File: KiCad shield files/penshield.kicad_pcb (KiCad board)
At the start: 2 copper layers, 55.9 x 16.5 mm, 7 parts

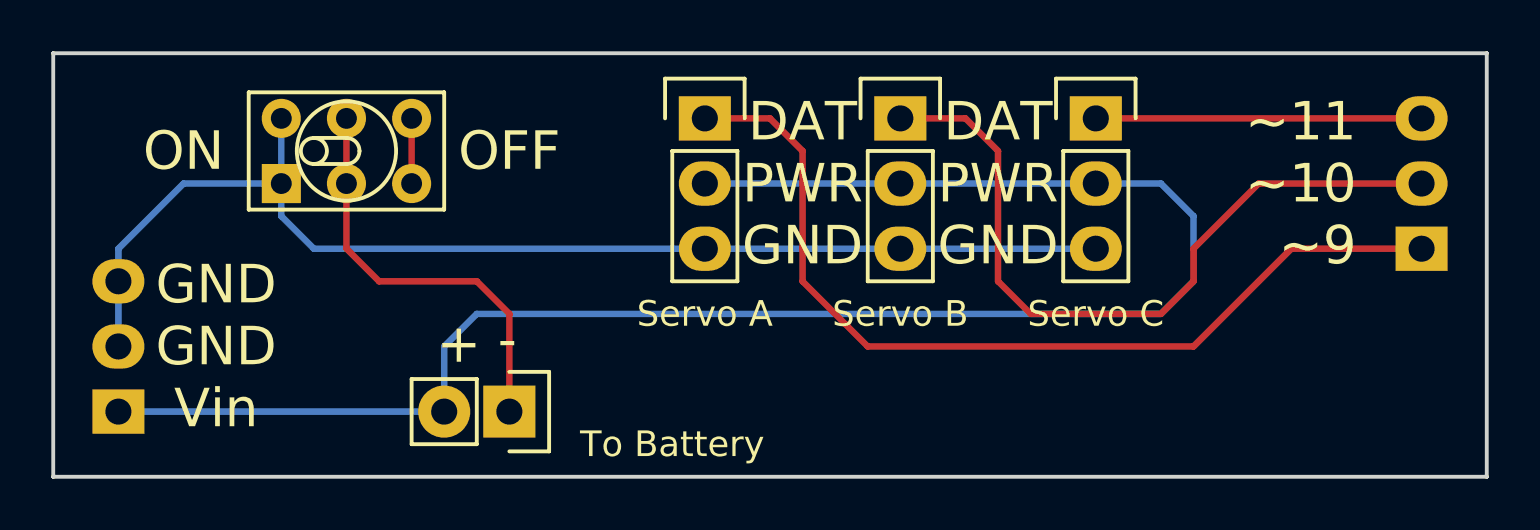
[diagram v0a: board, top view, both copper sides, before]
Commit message: Updated KiCad project; fixed spacing of header pins on shield
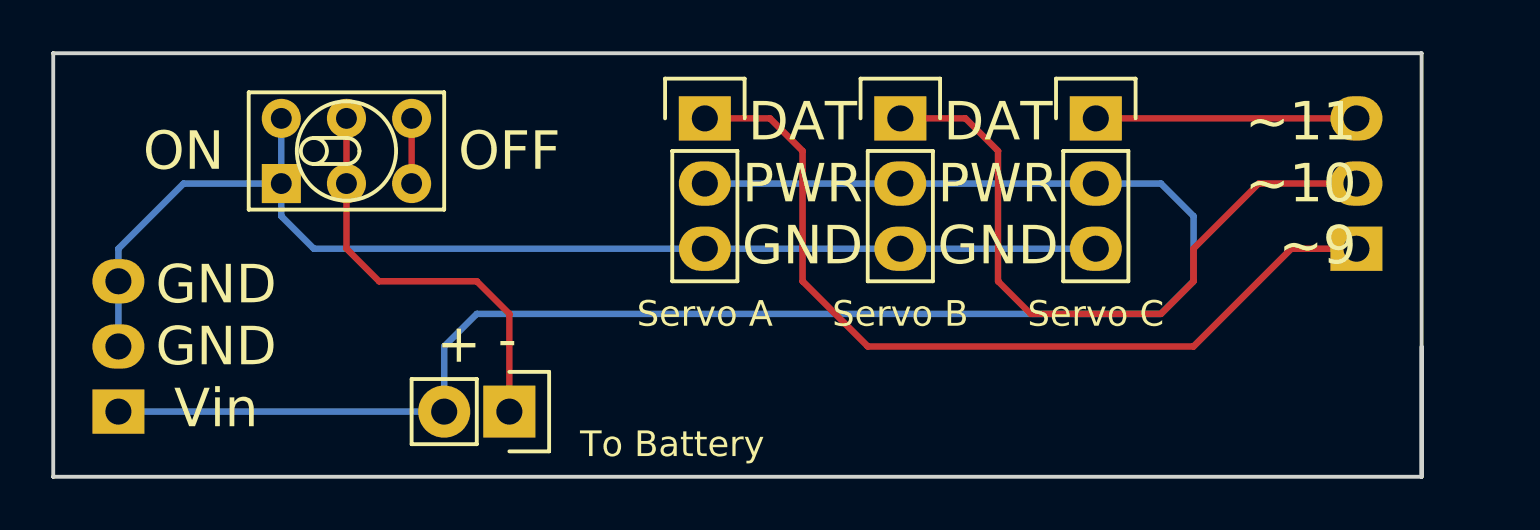
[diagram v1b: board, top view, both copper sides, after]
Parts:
- moved ? 2.54 mm to (188.0, 90.2)
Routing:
- net Net-(P2-Pad1): track 36.2 -> 33.6 mm
- net Net-(P3-Pad3): track 12.7 -> 10.2 mm
- net Net-(P3-Pad2): track 29.3 -> 26.8 mm
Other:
- board size 55.9 x 16.5 mm -> 53.3 x 16.5 mm
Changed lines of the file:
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@@
     (links 16)
     (no_connects 0)
-    (area 137.084999 78.8872 201.888991 103.8228)
+    (area 137.084999 78.8872 198.3728 103.8228)
     (thickness 1.6)
-    (drawings 11)
+    (drawings 12)
     (tracks 46)
     (zones 0)
@@
     (visible_elements 7FFFFFFF)
     (pcbplotparams
-      (layerselection 0x01030_80000001)
+      (layerselection 0x010f0_80000001)
       (usegerberextensions false)
       (excludeedgelayer true)
@@
       (drillshape 0)
       (scaleselection 1)
-      (outputdirectory gerb/))
+      (outputdirectory gerbers/))
   )
   (net 0 "")
@@
   )
   (module Pin_Headers:Pin_Header_Straight_1x03 (layer B.Cu)
-    (at 190.5 90.17)
+    (at 187.96 90.17)
     (descr "Through hole pin header")
     (tags "pin header")
@@
     )
   )
+  (gr_line (start 190.5 99.06) (end 137.16 99.06) (angle 90) (layer Edge.Cuts) (width 0.15))
+  (gr_line (start 190.5 99.06) (end 190.5 93.98) (angle 90) (layer Edge.Cuts) (width 0.15))
+  (gr_line (start 190.5 82.55) (end 190.5 99.06) (angle 90) (layer Edge.Cuts) (width 0.15))
   (gr_text "DAT\nPWR\nGND" (at 173.99 87.63) (layer F.SilkS)
     (effects (font (size 1.5 1.5) (thickness 0.3)))
@@
     (effects (font (size 1.5 1.5) (thickness 0.3)))
   )
-  (gr_line (start 193.04 82.55) (end 137.16 82.55) (angle 90) (layer Edge.Cuts) (width 0.15))
-  (gr_line (start 193.04 99.06) (end 193.04 82.55) (angle 90) (layer Edge.Cuts) (width 0.15))
-  (gr_line (start 137.16 99.06) (end 193.04 99.06) (angle 90) (layer Edge.Cuts) (width 0.15))
+  (gr_line (start 190.5 82.55) (end 137.16 82.55) (angle 90) (layer Edge.Cuts) (width 0.15))
   (gr_line (start 137.16 82.55) (end 137.16 99.06) (angle 90) (layer Edge.Cuts) (width 0.15))
   (segment (start 154.94 96.52) (end 154.94 92.71) (width 0.254) (layer F.Cu) (net 1))
@@
   (segment (start 170.18 87.63) (end 177.8 87.63) (width 0.254) (layer B.Cu) (net 2))
   (segment (start 170.18 87.63) (end 162.56 87.63) (width 0.254) (layer B.Cu) (net 2))
-  (segment (start 185.42 90.17) (end 190.5 90.17) (width 0.254) (layer F.Cu) (net 3))
+  (segment (start 187.96 90.17) (end 185.42 90.17) (width 0.254) (layer F.Cu) (net 3))
+  (segment (start 165.1 85.09) (end 162.56 85.09) (width 0.254) (layer F.Cu) (net 3))
+  (segment (start 165.1 85.09) (end 166.37 86.36) (width 0.254) (layer F.Cu) (net 3))
+  (segment (start 166.37 86.36) (end 166.37 91.44) (width 0.254) (layer F.Cu) (net 3))
+  (segment (start 166.37 91.44) (end 168.91 93.98) (width 0.254) (layer F.Cu) (net 3))
+  (segment (start 168.91 93.98) (end 181.61 93.98) (width 0.254) (layer F.Cu) (net 3))
+  (segment (start 181.61 93.98) (end 184.15 91.44) (width 0.254) (layer F.Cu) (net 3))
   (segment (start 184.15 91.44) (end 185.42 90.17) (width 0.254) (layer F.Cu) (net 3))
-  (segment (start 181.61 93.98) (end 184.15 91.44) (width 0.254) (layer F.Cu) (net 3))
-  (segment (start 168.91 93.98) (end 181.61 93.98) (width 0.254) (layer F.Cu) (net 3))
-  (segment (start 166.37 91.44) (end 168.91 93.98) (width 0.254) (layer F.Cu) (net 3))
-  (segment (start 166.37 86.36) (end 166.37 91.44) (width 0.254) (layer F.Cu) (net 3))
-  (segment (start 165.1 85.09) (end 166.37 86.36) (width 0.254) (layer F.Cu) (net 3))
-  (segment (start 162.56 85.09) (end 165.1 85.09) (width 0.254) (layer F.Cu) (net 3))
   (segment (start 170.18 90.17) (end 177.8 90.17) (width 0.254) (layer B.Cu) (net 4))
   (segment (start 162.56 90.17) (end 170.18 90.17) (width 0.254) (layer B.Cu) (net 4))
@@
   (segment (start 139.7 90.17) (end 142.24 87.63) (width 0.254) (layer B.Cu) (net 4))
   (segment (start 139.7 93.98) (end 139.7 91.44) (width 0.254) (layer B.Cu) (net 4))
-  (segment (start 170.18 85.09) (end 172.72 85.09) (width 0.254) (layer F.Cu) (net 5))
-  (segment (start 184.15 87.63) (end 190.5 87.63) (width 0.254) (layer F.Cu) (net 5))
+  (segment (start 187.96 87.63) (end 184.15 87.63) (width 0.254) (layer F.Cu) (net 5))
   (segment (start 181.61 90.17) (end 184.15 87.63) (width 0.254) (layer F.Cu) (net 5))
   (segment (start 181.61 91.44) (end 181.61 90.17) (width 0.254) (layer F.Cu) (net 5))
@@
   (segment (start 173.99 86.36) (end 173.99 91.44) (width 0.254) (layer F.Cu) (net 5))
   (segment (start 172.72 85.09) (end 173.99 86.36) (width 0.254) (layer F.Cu) (net 5))
-  (segment (start 177.8 85.09) (end 190.5 85.09) (width 0.254) (layer F.Cu) (net 6))
+  (segment (start 172.72 85.09) (end 170.18 85.09) (width 0.254) (layer F.Cu) (net 5))
+  (segment (start 177.8 85.09) (end 187.96 85.09) (width 0.254) (layer F.Cu) (net 6))
   (segment (start 151.13 85.09) (end 151.13 87.63) (width 0.254) (layer F.Cu) (net 7))
 )
